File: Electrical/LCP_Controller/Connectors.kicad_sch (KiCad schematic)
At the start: 8 parts, among them J10 Conn_01x04, J21 Conn_Coaxial, J22 Conn_01x04, J23 ANALOG_CONN, J24 Conn_01x04, J25 Conn_01x04, J26 Conn_01x04, J27 Conn_01x04

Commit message: Hardware Revision : v0.3
1. modified schematic design, removed unnecessary test points.
2. pcb layout 2x8 Inches allowance dimension, layout is in progress
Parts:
- renumbered J21 to J18, J23 to J19, J10 to J20, J25 to J21, J24 to J23, J26 to J24, J27 to J25
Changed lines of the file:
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@@
   (symbol (lib_id "Connector_Generic:Conn_02x04_Odd_Even") (at 171.45 46.99 0) (unit 1)
     (in_bom yes) (on_board yes)
-    (property "Reference" "J23" (id 0) (at 173.99 41.91 0)
+    (property "Reference" "J19" (id 0) (at 173.99 41.91 0)
       (effects (font (size 1.27 1.27)) (justify right))
     )
@@
   (symbol (lib_id "power:GND") (at 265.43 55.88 0) (unit 1)
     (in_bom yes) (on_board yes)
-    (property "Reference" "#PWR096" (id 0) (at 265.43 62.23 0)
+    (property "Reference" "#PWR0104" (id 0) (at 265.43 62.23 0)
       (effects (font (size 1.27 1.27)) hide)
     )
@@
   (symbol (lib_id "Connector_Generic:Conn_01x04") (at 274.32 50.8 0) (mirror x) (unit 1)
     (in_bom yes) (on_board yes)
-    (property "Reference" "J25" (id 0) (at 272.2372 40.005 0))
+    (property "Reference" "J21" (id 0) (at 272.2372 40.005 0))
     (property "Value" "Conn_01x04" (id 1) (at 272.2372 42.3164 0))
     (property "Footprint" "Connector_PinHeader_2.54mm:PinHeader_1x04_P2.54mm_Vertical" (id 2) (at 274.32 50.8 0)
@@
   (symbol (lib_id "power:GND") (at 78.74 182.88 0) (unit 1)
     (in_bom yes) (on_board yes)
-    (property "Reference" "#PWR093" (id 0) (at 78.74 189.23 0)
+    (property "Reference" "#PWR0106" (id 0) (at 78.74 189.23 0)
       (effects (font (size 1.27 1.27)) hide)
     )
@@
   (symbol (lib_id "Connector:Conn_Coaxial") (at 81.28 46.99 0) (unit 1)
     (in_bom yes) (on_board yes)
-    (property "Reference" "J21" (id 0) (at 83.82 47.625 0)
+    (property "Reference" "J18" (id 0) (at 83.82 47.625 0)
       (effects (font (size 1.27 1.27)) (justify left))
     )
@@
   (symbol (lib_id "power:GND") (at 81.28 54.61 0) (unit 1)
     (in_bom yes) (on_board yes)
-    (property "Reference" "#PWR094" (id 0) (at 81.28 60.96 0)
+    (property "Reference" "#PWR0103" (id 0) (at 81.28 60.96 0)
       (effects (font (size 1.27 1.27)) hide)
     )
@@
   (symbol (lib_id "Connector_Generic:Conn_01x04") (at 182.88 179.07 0) (mirror x) (unit 1)
     (in_bom yes) (on_board yes)
-    (property "Reference" "J24" (id 0) (at 182.88 170.18 0))
+    (property "Reference" "J23" (id 0) (at 182.88 170.18 0))
     (property "Value" "Conn_01x04" (id 1) (at 180.7972 170.5864 0)
       (effects (font (size 1.27 1.27)) hide)
@@
   (symbol (lib_id "power:GND") (at 173.99 182.88 0) (unit 1)
     (in_bom yes) (on_board yes)
-    (property "Reference" "#PWR095" (id 0) (at 173.99 189.23 0)
+    (property "Reference" "#PWR0107" (id 0) (at 173.99 189.23 0)
       (effects (font (size 1.27 1.27)) hide)
     )
@@
   (symbol (lib_id "Connector_Generic:Conn_01x04") (at 278.13 179.07 0) (mirror x) (unit 1)
     (in_bom yes) (on_board yes)
-    (property "Reference" "J26" (id 0) (at 278.13 170.18 0))
+    (property "Reference" "J24" (id 0) (at 278.13 170.18 0))
     (property "Value" "Conn_01x04" (id 1) (at 276.0472 170.5864 0)
       (effects (font (size 1.27 1.27)) hide)
@@
   (symbol (lib_id "power:GND") (at 269.24 182.88 0) (unit 1)
     (in_bom yes) (on_board yes)
-    (property "Reference" "#PWR097" (id 0) (at 269.24 189.23 0)
+    (property "Reference" "#PWR0108" (id 0) (at 269.24 189.23 0)
       (effects (font (size 1.27 1.27)) hide)
     )
@@
   (symbol (lib_id "Connector_Generic:Conn_01x04") (at 373.38 179.07 0) (mirror x) (unit 1)
     (in_bom yes) (on_board yes)
-    (property "Reference" "J27" (id 0) (at 373.38 170.18 0))
+    (property "Reference" "J25" (id 0) (at 373.38 170.18 0))
     (property "Value" "Conn_01x04" (id 1) (at 371.2972 170.5864 0)
       (effects (font (size 1.27 1.27)) hide)
@@
   (symbol (lib_id "power:GND") (at 364.49 182.88 0) (unit 1)
     (in_bom yes) (on_board yes)
-    (property "Reference" "#PWR098" (id 0) (at 364.49 189.23 0)
+    (property "Reference" "#PWR0109" (id 0) (at 364.49 189.23 0)
       (effects (font (size 1.27 1.27)) hide)
     )
@@
   (symbol (lib_id "Connector_Generic:Conn_01x04") (at 358.14 49.53 0) (mirror x) (unit 1)
     (in_bom yes) (on_board yes)
-    (property "Reference" "J10" (id 0) (at 356.0572 38.735 0))
+    (property "Reference" "J20" (id 0) (at 356.0572 38.735 0))
     (property "Value" "Conn_01x04" (id 1) (at 356.0572 41.0464 0))
     (property "Footprint" "Connector_JST:JST_SH_BM04B-SRSS-TB_1x04-1MP_P1.00mm_Vertical" (id 2) (at 358.14 49.53 0)
@@
   (symbol (lib_id "power:GND") (at 349.25 58.42 0) (unit 1)
     (in_bom yes) (on_board yes)
-    (property "Reference" "#PWR013" (id 0) (at 349.25 64.77 0)
-      (effects (font (size 1.27 1.27)) hide)
-    )
+    (property "Reference" "#PWR0105" (id 0) (at 349.25 64.77 0)
+      (effects (font (size 1.27 1.27)) hide)
+    )

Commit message: Hw Rev : 0.3v
changed buck-coverter LMR50410XDBVR to BD9G102G-LB, added schotty diode.
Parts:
- J18: MPN 132134-11 -> 132134-15
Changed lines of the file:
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@@
       (effects (font (size 1.27 1.27)) hide)
     )
-    (property "MPN" "132134-11" (id 4) (at 81.28 46.99 0)
+    (property "MPN" "132134-15" (id 4) (at 81.28 46.99 0)
       (effects (font (size 1.27 1.27)) hide)
     )

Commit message: Removed RF Switch
Deleted the RF Switch.

GPS Signal is routed to J17 and Iridium to J18.
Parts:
- J22: footprint Connector_PinHeader_2.54mm:PinHeader_1x04_P2.54mm_Vertical -> Connector_Molex:Molex_Micro-Fit_3.0_43045-0412_2x02_P3.00mm_Vertical

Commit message: GPS and Iridium Layout Finalized
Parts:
- J22: footprint Connector_Molex:Molex_Micro-Fit_3.0_43045-0412_2x02_P3.00mm_Vertical -> Connector_PinHeader_2.54mm:PinHeader_1x04_P2.54mm_Vertical
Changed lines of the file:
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@@
       (effects (font (size 1.27 1.27)) hide)
     )
-    (property "Footprint" "Connector_Molex:Molex_Micro-Fit_3.0_43045-0412_2x02_P3.00mm_Vertical" (at 87.63 179.07 0)
+    (property "Footprint" "Connector_PinHeader_2.54mm:PinHeader_1x04_P2.54mm_Vertical" (at 87.63 179.07 0)
       (effects (font (size 1.27 1.27)) hide)
     )

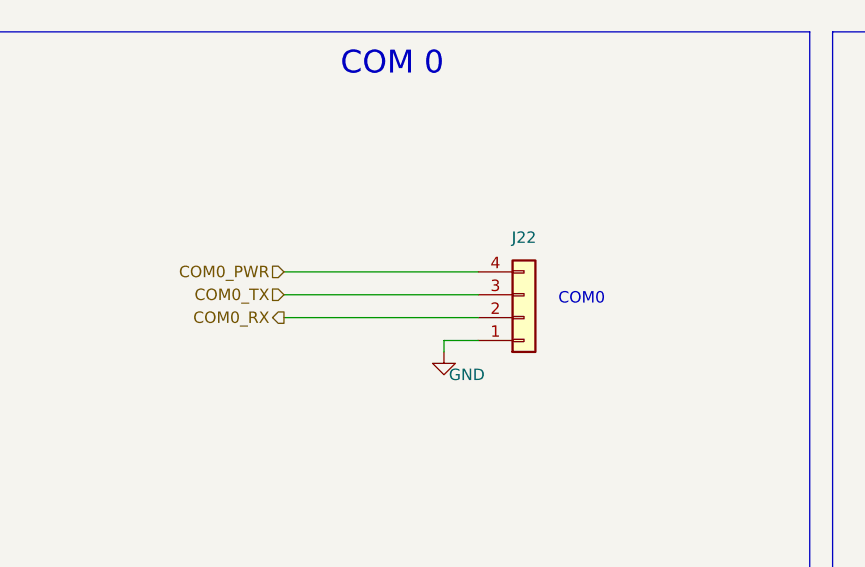
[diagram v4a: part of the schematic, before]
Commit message: Connector Progress
J2 J22 and J23 converted to Molex Microfit

SALEAE TEST connectors removed
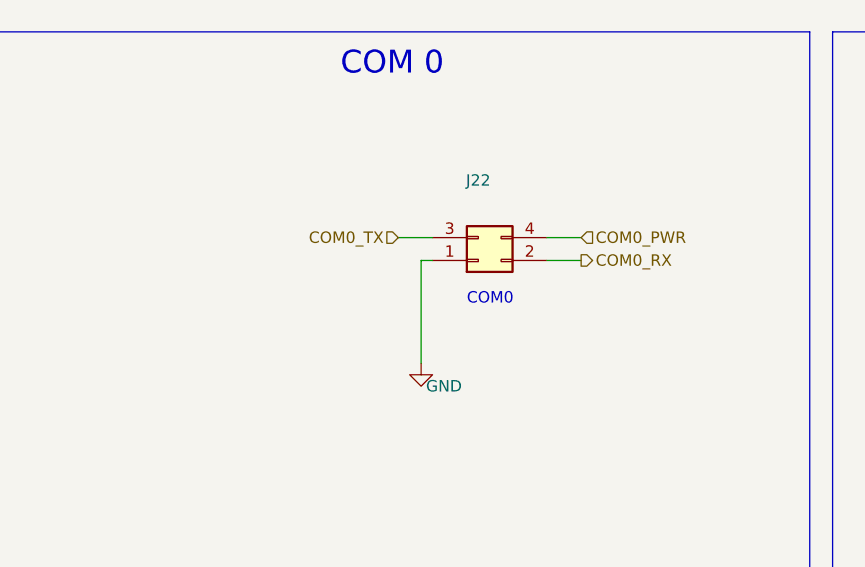
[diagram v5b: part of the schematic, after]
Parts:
- J22: footprint Connector_PinHeader_2.54mm:PinHeader_1x04_P2.54mm_Vertical -> Connector_Molex:Molex_Micro-Fit_3.0_43045-0412_2x02_P3.00mm_Vertical; symbol Connector_Generic:Conn_01x04 -> Connector_Generic:Conn_02x02_Odd_Even
- J23: footprint Connector_PinHeader_2.54mm:PinHeader_1x04_P2.54mm_Vertical -> Connector_Molex:Molex_Micro-Fit_3.0_43045-0412_2x02_P3.00mm_Vertical
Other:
- moved on the sheet: J22
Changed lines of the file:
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@@
+    (stroke (width 0) (type default))
+  )
+  (wire (pts (xy 90.17 172.72) (xy 93.98 172.72))
     (stroke (width 0) (type default))
   )
@@
     (stroke (width 0) (type default))
   )
-  (wire (pts (xy 78.74 181.61) (xy 82.55 181.61))
-    (stroke (width 0) (type default))
-  )
   (polyline (pts (xy 212.09 78.74) (xy 302.26 78.74))
     (stroke (width 0) (type default))
@@
     (stroke (width 0) (type default))
   )
+  (wire (pts (xy 76.2 172.72) (xy 76.2 184.15))
+    (stroke (width 0) (type default))
+  )
   (polyline (pts (xy 118.11 19.05) (xy 208.28 19.05))
     (stroke (width 0) (type default))
@@
     (stroke (width 0) (type default))
   )
-  (wire (pts (xy 60.96 179.07) (xy 82.55 179.07))
-    (stroke (width 0) (type default))
-  )
   (wire (pts (xy 269.24 181.61) (xy 273.05 181.61))
     (stroke (width 0) (type default))
@@
     (stroke (width 0) (type default))
   )
-  (wire (pts (xy 60.96 173.99) (xy 82.55 173.99))
-    (stroke (width 0) (type default))
-  )
   (wire (pts (xy 336.55 44.45) (xy 353.06 44.45))
     (stroke (width 0) (type default))
   )
-  (wire (pts (xy 78.74 182.88) (xy 78.74 181.61))
-    (stroke (width 0) (type default))
-  )
   (wire (pts (xy 269.24 53.34) (xy 265.43 53.34))
     (stroke (width 0) (type default))
@@
     (stroke (width 0) (type default))
   )
+  (wire (pts (xy 73.66 170.18) (xy 77.47 170.18))
+    (stroke (width 0) (type default))
+  )
   (polyline (pts (xy 309.88 147.32) (xy 309.88 207.01))
     (stroke (width 0) (type default))
@@
     (stroke (width 0) (type default))
   )
+  (wire (pts (xy 77.47 172.72) (xy 76.2 172.72))
+    (stroke (width 0) (type default))
+  )
   (wire (pts (xy 76.2 46.99) (xy 67.31 46.99))
     (stroke (width 0) (type default))
@@
     (stroke (width 0) (type default))
   )
-  (wire (pts (xy 60.96 176.53) (xy 82.55 176.53))
+  (wire (pts (xy 90.17 170.18) (xy 93.98 170.18))
     (stroke (width 0) (type default))
   )
@@
     (stroke (width 0) (type default))
   )
-  (text "COM0" (at 91.44 177.8 0)
+  (text "COM0" (at 81.28 177.8 0)
     (effects (font (size 1.27 1.27)) (justify left bottom))
   )
@@
     (effects (font (size 1.27 1.27)) (justify right))
   )
-  (hierarchical_label "COM0_RX" (shape output) (at 60.96 179.07 180) (fields_autoplaced)
-    (effects (font (size 1.27 1.27)) (justify right))
+  (hierarchical_label "COM0_RX" (shape output) (at 93.98 172.72 0) (fields_autoplaced)
+    (effects (font (size 1.27 1.27)) (justify left))
   )
   (hierarchical_label "COM1_PWR" (shape input) (at 156.21 173.99 180) (fields_autoplaced)
     (effects (font (size 1.27 1.27)) (justify right))
   )
-  (hierarchical_label "COM0_TX" (shape input) (at 60.96 176.53 180) (fields_autoplaced)
+  (hierarchical_label "COM0_TX" (shape input) (at 73.66 170.18 180) (fields_autoplaced)
     (effects (font (size 1.27 1.27)) (justify right))
   )
@@
     (effects (font (size 1.27 1.27)) (justify right))
   )
-  (hierarchical_label "COM0_PWR" (shape input) (at 60.96 173.99 180) (fields_autoplaced)
-    (effects (font (size 1.27 1.27)) (justify right))
+  (hierarchical_label "COM0_PWR" (shape input) (at 93.98 170.18 0) (fields_autoplaced)
+    (effects (font (size 1.27 1.27)) (justify left))
   )
   (hierarchical_label "ADC24_IN3" (shape output) (at 149.86 52.07 180) (fields_autoplaced)
@@
     )
   )
-  (symbol (lib_id "Connector_Generic:Conn_01x04") (at 87.63 179.07 0) (mirror x) (unit 1)
-    (in_bom yes) (on_board yes) (dnp no)
-    (property "Reference" "J22" (at 87.63 170.18 0)
-      (effects (font (size 1.27 1.27)))
-    )
-    (property "Value" "Conn_01x04" (at 85.5472 170.5864 0)
-      (effects (font (size 1.27 1.27)) hide)
-    )
-    (property "Footprint" "Connector_PinHeader_2.54mm:PinHeader_1x04_P2.54mm_Vertical" (at 87.63 179.07 0)
-      (effects (font (size 1.27 1.27)) hide)
-    )
-    (property "Datasheet" "~" (at 87.63 179.07 0)
-      (effects (font (size 1.27 1.27)) hide)
-    )
-    (property "MPN" "" (at 87.63 179.07 0)
+  (symbol (lib_id "Connector_Generic:Conn_02x02_Odd_Even") (at 82.55 172.72 0) (mirror x) (unit 1)
+    (in_bom yes) (on_board yes) (dnp no)
+    (property "Reference" "J22" (at 82.55 163.83 0)
+      (effects (font (size 1.27 1.27)))
+    )
+    (property "Value" "Conn_01x04" (at 80.4672 164.2364 0)
+      (effects (font (size 1.27 1.27)) hide)
+    )
+    (property "Footprint" "Connector_Molex:Molex_Micro-Fit_3.0_43045-0412_2x02_P3.00mm_Vertical" (at 82.55 172.72 0)
+      (effects (font (size 1.27 1.27)) hide)
+    )
+    (property "Datasheet" "~" (at 82.55 172.72 0)
+      (effects (font (size 1.27 1.27)) hide)
+    )
+    (property "MPN" "" (at 82.55 172.72 0)
       (effects (font (size 1.27 1.27)) hide)
     )
@@
     )
   )
-  (symbol (lib_id "power:GND") (at 78.74 182.88 0) (unit 1)
-    (in_bom yes) (on_board yes) (dnp no)
-    (property "Reference" "#PWR0106" (at 78.74 189.23 0)
-      (effects (font (size 1.27 1.27)) hide)
-    )
-    (property "Value" "GND" (at 81.28 185.42 0)
-      (effects (font (size 1.27 1.27)))
-    )
-    (property "Footprint" "" (at 78.74 182.88 0)
-      (effects (font (size 1.27 1.27)) hide)
-    )
-    (property "Datasheet" "" (at 78.74 182.88 0)
+  (symbol (lib_id "power:GND") (at 76.2 184.15 0) (unit 1)
+    (in_bom yes) (on_board yes) (dnp no)
+    (property "Reference" "#PWR0106" (at 76.2 190.5 0)
+      (effects (font (size 1.27 1.27)) hide)
+    )
+    (property "Value" "GND" (at 78.74 186.69 0)
+      (effects (font (size 1.27 1.27)))
+    )
+    (property "Footprint" "" (at 76.2 184.15 0)
+      (effects (font (size 1.27 1.27)) hide)
+    )
+    (property "Datasheet" "" (at 76.2 184.15 0)
       (effects (font (size 1.27 1.27)) hide)
     )
@@
       (effects (font (size 1.27 1.27)) hide)
     )
-    (property "Footprint" "Connector_PinHeader_2.54mm:PinHeader_1x04_P2.54mm_Vertical" (at 182.88 179.07 0)
-      (effects (font (size 1.27 1.27)) hide)
-    )
+    (property "Footprint" "Connector_Molex:Molex_Micro-Fit_3.0_43045-0412_2x02_P3.00mm_Vertical" (at 182.88 179.07 0)
+      (effects (font (size 1.27 1.27)) hide)
+    )

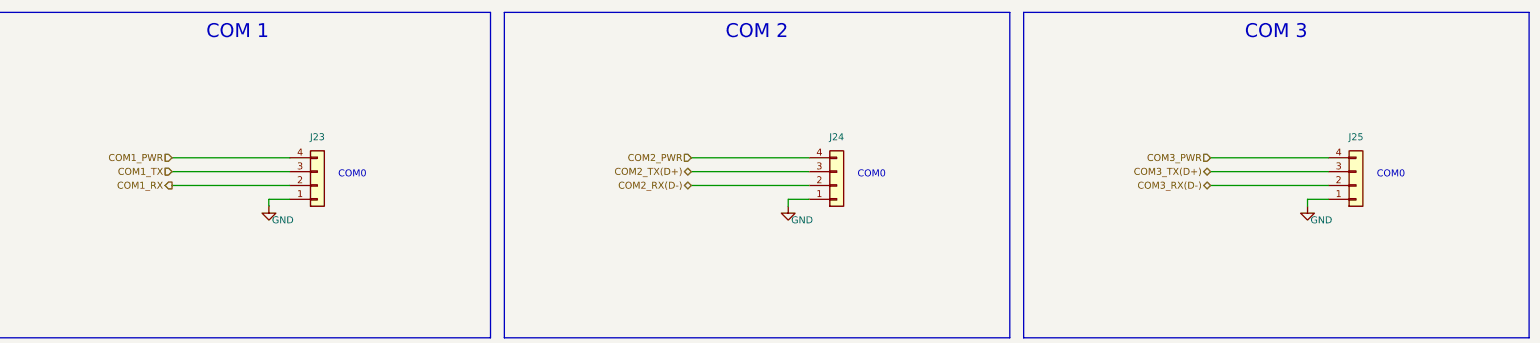
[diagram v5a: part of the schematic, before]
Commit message: Completed Board Mods
COM 0, 1, 2, 3 are now microfit.

Control Board I2C Interconnect

Separated from PWR and now microfit.

RN2 changed to 4k7.

J3, J9, J12, J16 are removed.

U8 circuit moved under IMU footprint.

C11 and C13 moved between IMU and Iridium.

GPS moved from underneath Iridium.
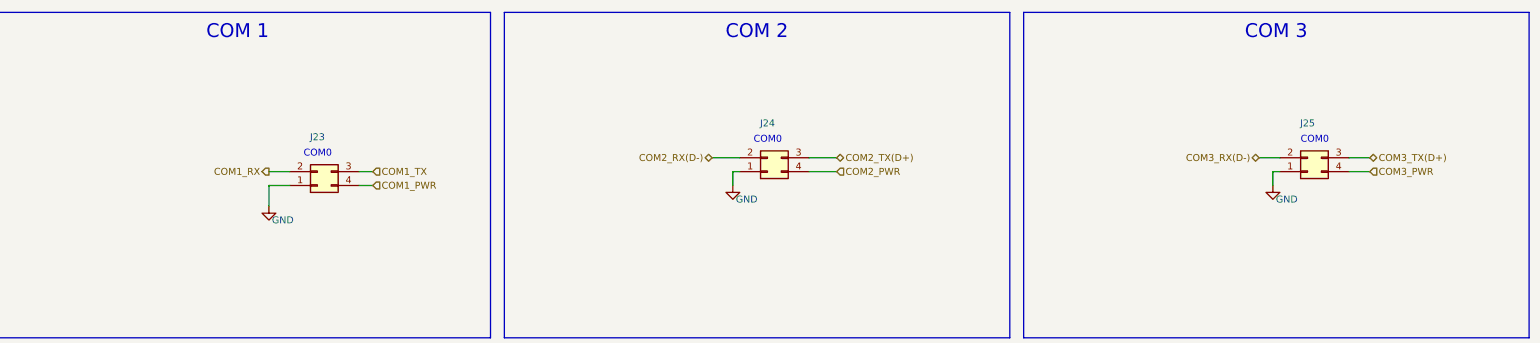
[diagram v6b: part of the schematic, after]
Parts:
- J23: symbol Connector_Generic:Conn_01x04 -> Connector_Generic:Conn_02x02_Counter_Clockwise
- J24, J25: footprint Connector_PinHeader_2.54mm:PinHeader_1x04_P2.54mm_Vertical -> Connector_Molex:Molex_Micro-Fit_3.0_43045-0412_2x02_P3.00mm_Vertical; symbol Connector_Generic:Conn_01x04 -> Connector_Generic:Conn_02x02_Counter_Clockwise
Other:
- moved on the sheet: J23, J24, J25

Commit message: Board Revision 0.4
Completed
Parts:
- J22, J23, J24, J25: MPN (none) -> 0430450428
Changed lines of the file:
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@@
   (title_block
     (title "LCP Controller ")
-    (date "2022-12-19")
-    (rev "0.3")
+    (date "2024-07-22")
+    (rev "0.4")
     (company "NOAA Pacific Marine Environmental Laboratory")
-    (comment 3 "Current design modified by: Basharat Basharat")
+    (comment 1 "https://github.com/PaulZC/Artemis_Global_Tracker")
+    (comment 2 "Based on Paul Clark's Sparkfun Artemis Global Tracker")
+    (comment 3 "Current Design Updated by: Joseph Kurina")
     (comment 4 "Current design by: Matt Casari")
     (comment 5 "Current design modified by: Basharat Martin")
+    (comment 6 "Current Design Updated by: Joseph Kurina")
   )
   (junction (at 184.15 46.99) (diameter 0) (color 0 0 0 0)
@@
       (effects (font (size 1.27 1.27)) hide)
     )
-    (property "MPN" "" (at 82.55 172.72 0)
+    (property "MPN" "0430450428" (at 82.55 172.72 0)
       (effects (font (size 1.27 1.27)) hide)
     )
@@
       (effects (font (size 1.27 1.27)) hide)
     )
-    (property "MPN" "" (at 182.88 179.07 0)
+    (property "MPN" "0430450428" (at 182.88 179.07 0)
       (effects (font (size 1.27 1.27)) hide)
     )
@@
       (effects (font (size 1.27 1.27)) hide)
     )
-    (property "MPN" "" (at 265.43 176.53 0)
+    (property "MPN" "0430450428" (at 265.43 176.53 0)
       (effects (font (size 1.27 1.27)) hide)
     )
@@
       (effects (font (size 1.27 1.27)) hide)
     )
-    (property "MPN" "" (at 364.49 176.53 0)
-      (effects (font (size 1.27 1.27)) hide)
-    )
+    (property "MPN" "0430450428" (at 364.49 176.53 0)
+      (effects (font (size 1.27 1.27)) hide)
+    )

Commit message: New Layout
Changes for this Rev:
- Impedance Matched GPS traces
- Copper Pours
- Vias/Traces changed to bring down costs
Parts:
- removed J18: Conn_Coaxial, Connector_Coaxial:SMA_Amphenol_132134_Vertical, symbol Connector:Conn_Coaxial
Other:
- note removed: "Iridium/GPS Coax"
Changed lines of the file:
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@@
-    (stroke (width 0) (type default))
-  )
-  (wire (pts (xy 76.2 46.99) (xy 67.31 46.99))
     (stroke (width 0) (type default))
   )
@@
   )
   (wire (pts (xy 372.11 173.99) (xy 375.92 173.99))
-    (stroke (width 0) (type default))
-  )
-  (wire (pts (xy 81.28 54.61) (xy 81.28 52.07))
     (stroke (width 0) (type default))
   )
@@
     (effects (font (size 2.54 2.54)) (justify right bottom))
   )
-  (text "Iridium/GPS Coax" (at 83.82 24.13 0)
-    (effects (font (size 2.54 2.54)) (justify right bottom))
-  )
   (hierarchical_label "SPARE_I2C_SDA" (shape bidirectional) (at 245.11 50.8 180) (fields_autoplaced)
     (effects (font (size 1.27 1.27)) (justify right))
@@
   )
   (hierarchical_label "SPARE_I2C_PWR" (shape bidirectional) (at 245.11 45.72 180) (fields_autoplaced)
-    (effects (font (size 1.27 1.27)) (justify right))
-  )
-  (hierarchical_label "Iridium_GPS_Signal" (shape bidirectional) (at 67.31 46.99 180) (fields_autoplaced)
     (effects (font (size 1.27 1.27)) (justify right))
   )
@@
         )
       )
-    )
-  )
-  (symbol (lib_id "Connector:Conn_Coaxial") (at 81.28 46.99 0) (unit 1)
-    (in_bom yes) (on_board yes) (dnp no)
-    (property "Reference" "J18" (at 83.82 47.625 0)
-      (effects (font (size 1.27 1.27)) (justify left))
-    )
-    (property "Value" "Conn_Coaxial" (at 83.82 49.9364 0)
-      (effects (font (size 1.27 1.27)) (justify left))
-    )
-    (property "Footprint" "Connector_Coaxial:SMA_Amphenol_132134_Vertical" (at 81.28 46.99 0)
-      (effects (font (size 1.27 1.27)) hide)
-    )
-    (property "Datasheet" " ~" (at 81.28 46.99 0)
-      (effects (font (size 1.27 1.27)) hide)
-    )
-    (property "MPN" "132134-15" (at 81.28 46.99 0)
-      (effects (font (size 1.27 1.27)) hide)
-    )
-    (pin "1")
-    (pin "2")
-    (instances
-      (project "LCP_Controller"
-        (path "/df0f358a-57ab-4ee9-8b36-6ce64ef9d813/00000000-0000-0000-0000-00005ee033be"
-          (reference "J18") (unit 1)
-        )
-      )
-    )
-  )
-  (symbol (lib_id "power:GND") (at 81.28 54.61 0) (unit 1)
-    (in_bom yes) (on_board yes) (dnp no)
-    (property "Reference" "#PWR0103" (at 81.28 60.96 0)
-      (effects (font (size 1.27 1.27)) hide)
-    )
-    (property "Value" "GND" (at 83.82 57.15 0)
-      (effects (font (size 1.27 1.27)))
-    )
-    (property "Footprint" "" (at 81.28 54.61 0)
-      (effects (font (size 1.27 1.27)) hide)
-    )
-    (property "Datasheet" "" (at 81.28 54.61 0)
-      (effects (font (size 1.27 1.27)) hide)
-    )
-    (pin "1")
-    (instances
-      (project "LCP_Controller"
-        (path "/df0f358a-57ab-4ee9-8b36-6ce64ef9d813/00000000-0000-0000-0000-00005ee033be"
-          (reference "#PWR0103") (unit 1)
-        )
-      )
